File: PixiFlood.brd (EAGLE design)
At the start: 47 x 47 mm, 31 parts, among them IC1 78L05Z, IC2 WS2811-SOP8, IC3 TC7W04FTC7W04F, U1 PT4115PT4115B89E, U2 PT4115PT4115B89E, U3 PT4115PT4115B89E, X1 22-23-2031, X2 LED-PAD, X3 LED-PAD, X4 22-23-2031, X5 LED-PAD, X6 LED-PAD, X7 LED-PAD, X8 LED-PAD

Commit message: Reworked and retitled to PixiFlood
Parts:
- D1, D2, D3: value (none) -> 1N5819
- IC2: value WS2811-SOP8 -> WS2811SOP8; device MyLibrary:SO08-SKINNYPADS -> drivers:SOP08-P-1.27
- IC3: value TC7W04FTC7W04F -> TC7W04F; device MyLibrary:SO08 -> logic:SOP08-P-1.27
- L1, L2, L3: value SLF7045 -> 82114R; device inductors:SLF7045 -> inductors:82114R
- R1, R6: device resistor:R1206 -> resistor:0204/5
- R2, R3, R4: device rcl:M0805 -> rcl:0204/5
- R5: device resistor:M1206 -> resistor:0204/5
- U1, U2, U3: value PT4115PT4115B89E -> PT4115B89E; device IC:SOT89-5 -> drivers:SOT89-5
- moved C1 24.6 mm to (43.7, 35.9), turned to 180 degrees
- moved L3 3.05 mm to (35.6, 7.49), turned to 90 degrees
- moved L1 2.84 mm to (35.3, 23.1), turned to 90 degrees
- moved L2 2.81 mm to (35.4, 15.4), turned to 90 degrees
- moved IC1 2.22 mm to (43.8, 39.9), turned to 270 degrees
- moved R6 2.18 mm to (19.2, 7.95)
- moved R5 1.82 mm to (19.3, 15.8)
- moved C2 1.73 mm to (38.5, 40.8)
- moved R3 1.48 mm to (34.0, 37.5)
- moved X1 1.27 mm to (24.1, 42.5)
- moved X4 1.02 mm to (32.0, 42.5)
- moved R1 0.76 mm to (21.1, 25.5)
- moved R2 0.65 mm to (27.1, 38.1)
- moved IC2 0.51 mm to (34.3, 33.8)
- moved R4 0.51 mm to (34.3, 30.0)
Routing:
- net +12V: track 87.5 -> 93.9 mm
- net RED: track 19.2 -> 23.6 mm, vias 2 -> 0
- net N$19: track 31.8 -> 27.6 mm
- net BLUE: track 23.7 -> 20.0 mm
- net N$10: track 42.6 -> 38.9 mm
- net N$9: track 57.4 -> 54.0 mm
- net GREEN: track 21.3 -> 18.0 mm
- net ROUT: track 45.2 -> 48.1 mm
- net N$1: track 8.89 -> 6.73 mm
- net N$7: track 3.88 -> 1.93 mm
- net N$2: track 8.80 -> 6.94 mm
- net +5V: track 51.7 -> 53.6 mm
- net N$5: track 8.67 -> 6.84 mm
- net N$3: track 63.9 -> 62.1 mm
- net GOUT: track 49.0 -> 50.2 mm
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
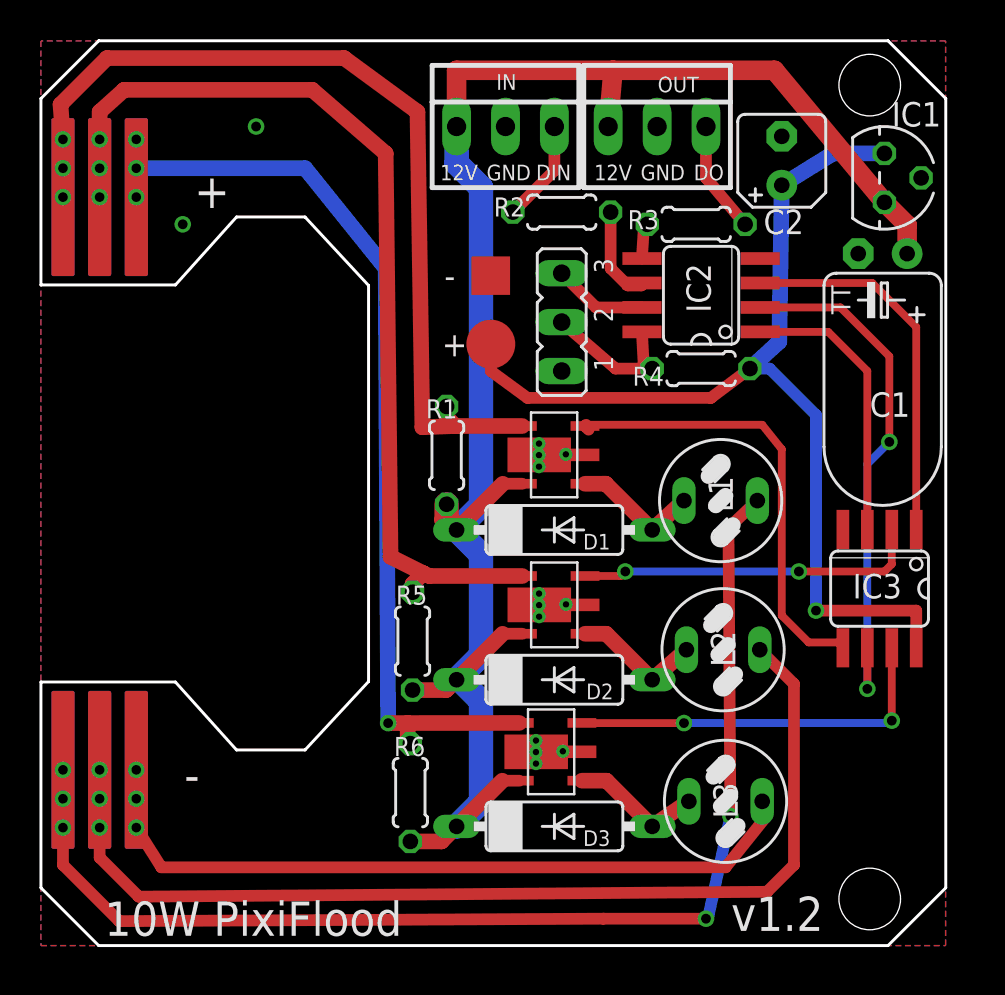
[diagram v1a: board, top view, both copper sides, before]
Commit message: Reworked and retitled to PixiFlood SMD
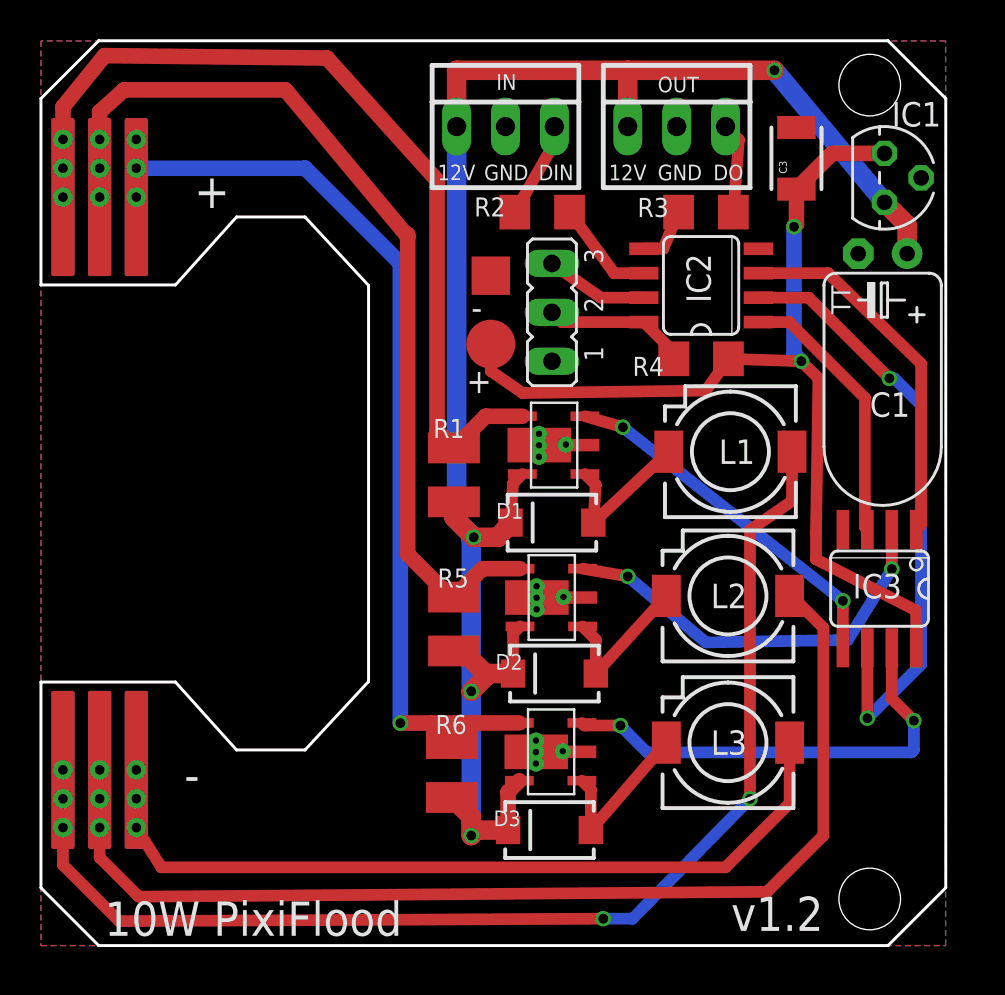
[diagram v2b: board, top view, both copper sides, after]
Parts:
- removed C2: .1uF, resistor:B45181A
- added C3: .1uF, SparkFun-Capacitors:1210
- D1, D2, D3: value 1N5819 -> B340A; device diode:DO07 -> SparkFun-DiscreteSemi:SMA-DIODE
- IC1: value 78L05Z -> AS78L05ZTR-E1
- IC2: value WS2811SOP8 -> WS2811-SOP8; device drivers:SOP08-P-1.27 -> MyLibrary:SO08-SKINNYPADS
- IC3: value TC7W04F -> TC7W04FTC7W04F; device logic:SOP08-P-1.27 -> MyLibrary:SO08
- L1, L2, L3: value 82114R -> SLF7045T-101MR60-H; device inductors:82114R -> inductors:SLF7045
- R1, R6: value .3ohm .25w -> .3ohm .5w; device resistor:0204/5 -> resistor:R1210
- R2, R3, R4: device rcl:0204/5 -> rcl:R1206
- R5: value .3hm .25w -> .3hm .5w; device resistor:0204/5 -> resistor:R1210
- U1, U2, U3: value PT4115B89E -> PT4115PT4115B89E; device drivers:SOT89-5 -> IC:SOT89-5
- moved L3 3.05 mm to (35.7, 10.5), turned to 0 degrees
- moved L2 2.81 mm to (35.7, 18.2), turned to 0 degrees
- moved L1 2.59 mm to (35.8, 25.7), turned to 0 degrees
- moved R6 2.44 mm to (21.3, 9.09)
- moved R5 2.33 mm to (21.5, 16.7)
- moved R1 1.09 mm to (21.5, 24.4)
- moved X4 1.02 mm to (33.0, 42.5)
- moved R2 1.02 mm to (26.0, 38.1)
- moved R3 0.81 mm to (34.5, 38.1)
- moved JP1 0.72 mm to (26.5, 32.9)
- moved IC2 0.51 mm to (34.3, 34.3)
- moved R4 0.51 mm to (34.3, 30.5)
- moved U1 0.51 mm to (26.7, 26.1)
- moved D1 0.40 mm to (26.5, 22.0), turned to 180 degrees
- moved U2 0.40 mm to (26.5, 18.2)
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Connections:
- net +5V: now also C3.1; no longer C2.+
- net GND: now also C3.2; no longer C2.-
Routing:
- net RED: track 23.6 -> 19.0 mm, vias 0 -> 2
- net N$19: track 27.6 -> 31.8 mm
- net BLUE: track 20.0 -> 23.7 mm
- net N$10: track 38.9 -> 42.6 mm
- net N$9: track 54.0 -> 57.4 mm
- net GREEN: track 18.0 -> 21.5 mm
- net +5V: track 53.6 -> 51.7 mm, vias 1 -> 2
- net N$2: track 6.94 -> 8.76 mm
- net GOUT: track 50.2 -> 48.4 mm
- net N$3: track 62.1 -> 63.6 mm
- net N$1: track 6.73 -> 8.14 mm
- net N$5: track 6.84 -> 8.18 mm
- net ROUT: track 48.1 -> 46.7 mm
- net N$7: track 1.93 -> 3.07 mm
- net N$4: track 5.82 -> 4.74 mm
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
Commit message: Reworked layout
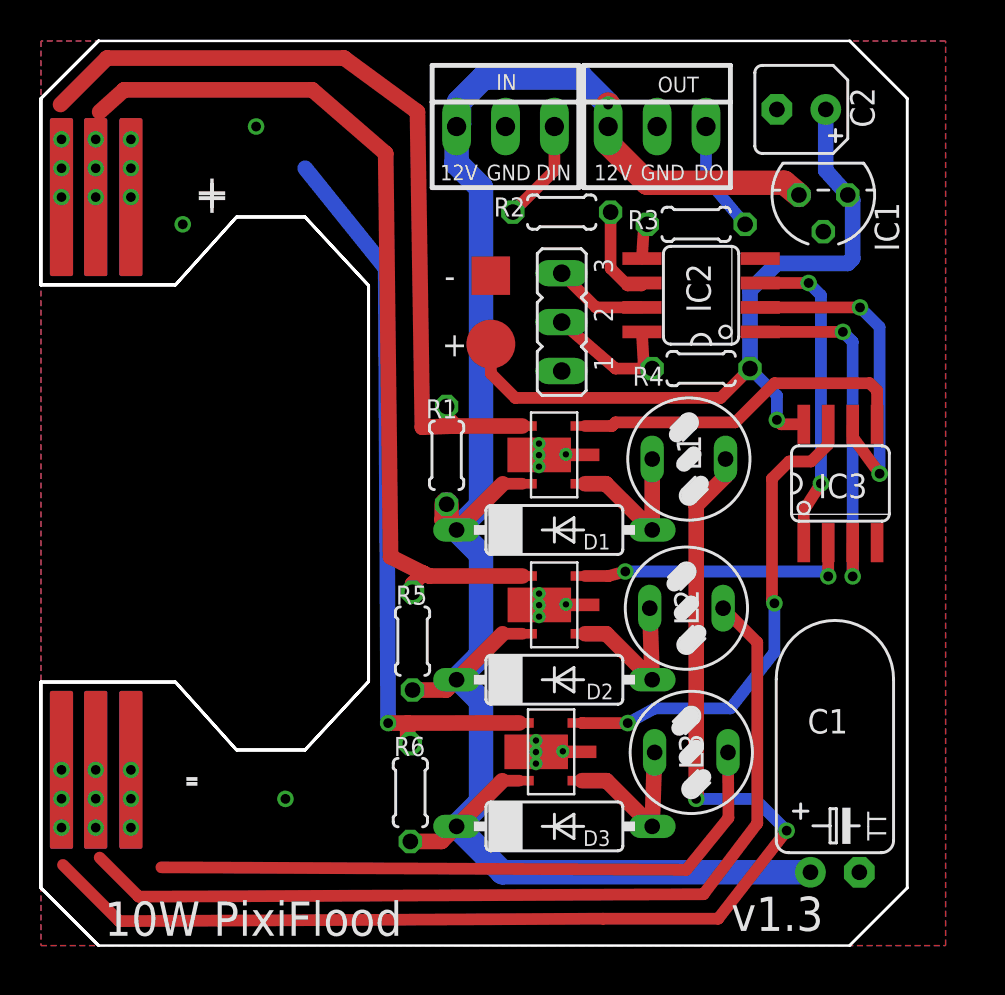
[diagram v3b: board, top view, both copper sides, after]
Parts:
- removed C3: .1uF, SparkFun-Capacitors:1210
- removed X2, X3, X5, X6, X7, X8: LED-PAD, MyLibrary:LED-PAD
- added B1: LED-BOARDV2, special:LED-BOARD_V2
- added C2: .1uF, resistor:B45181A
- D1, D2, D3: value B340A -> 1N5819; device SparkFun-DiscreteSemi:SMA-DIODE -> diode:DO07
- IC1: value AS78L05ZTR-E1 -> 78L05Z
- IC2: value WS2811-SOP8 -> WS2811SOP8; device MyLibrary:SO08-SKINNYPADS -> drivers:SOP08-P-1.27
- IC3: value TC7W04FTC7W04F -> TC7W04F; device MyLibrary:SO08 -> logic:SOP08-P-1.27
- L1, L2, L3: value SLF7045T-101MR60-H -> 82114R; device inductors:SLF7045 -> inductors:82114R
- R1, R6: value .3ohm .5w -> .3ohm .25w; device resistor:R1210 -> resistor:0204/5
- R2, R3, R4: device rcl:R1206 -> rcl:0204/5
- R5: value .3hm .5w -> .3hm .25w; device resistor:R1210 -> resistor:0204/5
- U1, U2, U3: value PT4115PT4115B89E -> PT4115B89E; device IC:SOT89-5 -> drivers:SOT89-5
- moved C1 32.2 mm to (41.2, 3.81), turned to 0 degrees
- moved IC3 5.83 mm to (41.5, 24.0), turned to 0 degrees
- moved IC1 3.30 mm to (40.6, 39.0), turned to 180 degrees
- moved R6 2.44 mm to (19.2, 7.95)
- moved R5 2.33 mm to (19.3, 15.8)
- moved L2 2.25 mm to (33.5, 17.5), turned to 90 degrees
- moved L1 2.19 mm to (33.7, 25.3), turned to 90 degrees
- moved L3 1.97 mm to (33.8, 10.0), turned to 90 degrees
- moved R1 1.09 mm to (21.1, 25.5)
- moved X4 1.02 mm to (32.0, 42.5)
- moved R2 1.02 mm to (27.1, 38.1)
- moved R3 0.81 mm to (34.0, 37.5)
- moved JP1 0.72 mm to (27.1, 32.4)
- moved IC2 0.51 mm to (34.3, 33.8)
- moved R4 0.51 mm to (34.3, 30.0)
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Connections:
- net +5V: now also C2.+; no longer C3.1
- net BOUT: now also B1.P$5@1, B1.P$5@2, B1.P$5@3; no longer X7.P$1@1, X7.P$1@2, X7.P$1@3
- net GND: now also C2.-; no longer C3.2
- net GOUT: now also B1.P$3@1, B1.P$3@2, B1.P$3@3; no longer X5.P$1@1, X5.P$1@2, X5.P$1@3
- net N$10: now also B1.P$6@1, B1.P$6@2, B1.P$6@3; no longer X8.P$1@1, X8.P$1@2, X8.P$1@3
- net N$3: now also B1.P$2@1, B1.P$2@2, B1.P$2@3; no longer X3.P$1@1, X3.P$1@2, X3.P$1@3
- net N$9: now also B1.P$4@1, B1.P$4@2, B1.P$4@3; no longer X6.P$1@1, X6.P$1@2, X6.P$1@3
- net ROUT: now also B1.P$1@1, B1.P$1@2, B1.P$1@3; no longer X2.P$1@1, X2.P$1@2, X2.P$1@3
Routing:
- net N$19: track 31.8 -> 17.3 mm
- net +5V: track 51.7 -> 39.3 mm, vias 2 -> 1
- net BOUT: track 50.1 -> 38.2 mm
- net N$9: track 57.4 -> 48.7 mm
- net N$10: track 42.6 -> 34.1 mm
- net +12V: track 93.6 -> 102.0 mm, vias 4 -> 1
- net GREEN: track 21.5 -> 14.5 mm
- net N$15: track 14.1 -> 19.0 mm, vias 0 -> 2
- net ROUT: track 46.7 -> 43.2 mm
- net GOUT: track 48.4 -> 45.8 mm
- net N$16: track 19.1 -> 16.5 mm, vias 0 -> 2
- net BLUE: track 23.7 -> 25.4 mm
- net N$7: track 3.07 -> 1.93 mm
- net N$4: track 4.74 -> 5.82 mm
- net N$3: track 63.6 -> 64.7 mm
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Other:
- board size 47 x 47 mm -> 45 x 47 mm
- board text added: "v1.3"
- board text removed: "v1.2"

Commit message: Reworked layout
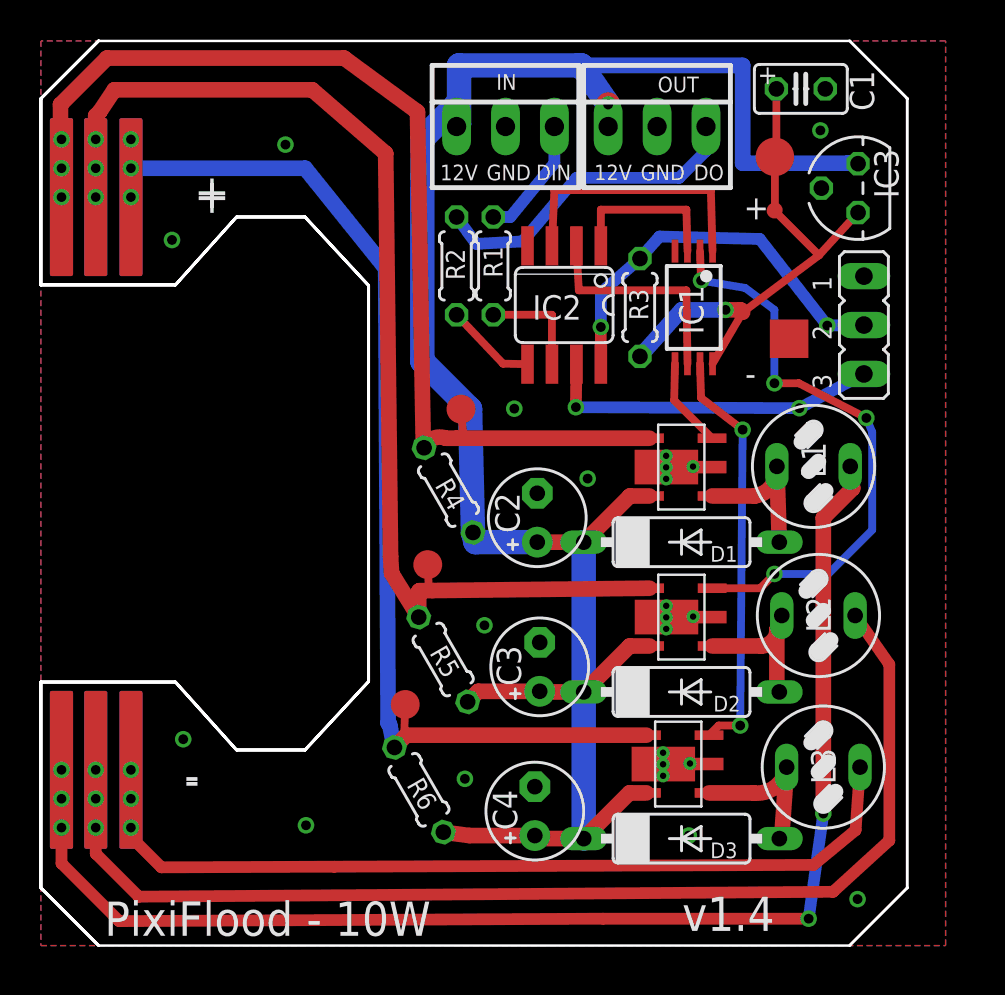
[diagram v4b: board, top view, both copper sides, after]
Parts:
- added C3, C4: 10uF, adafruit:E2,5-5
- added TP3, TP5, TP7: TPSQTP15R, testpad:TP15R
- C1: value EL 100uF -> .1uF; device rcl:TT2D6L -> capacitors:C025X050P
- C2: value .1uF -> 10uF; device resistor:B45181A -> adafruit:E2,5-5
- IC1: value 78L05Z -> TC7W04FP-0.65; device linear:TO92 -> logic:TSSOP8
- IC3: value TC7W04F -> 78L05Z; device logic:SOP08-P-1.27 -> linear:TO92
- R1: value .3ohm .25w -> 33R; device resistor:0204/5 -> rcl:0204/5
- R3: value 33R -> 100ohm
- R4: value 100ohm -> .3ohm .25w; device rcl:0204/5 -> resistor:0204/5
- TP1: value TPB2,54 -> TPSQTP20R; device testpad:B2,54 -> testpad:TP20R
- TP2: value PTR1TP20SQ -> TPSQTP20SQ
- moved C1 40.7 mm to (39.5, 44.5)
- moved C2 25.3 mm to (25.8, 22.2), turned to 90 degrees
- moved TP1 17.7 mm to (38.1, 41.0)
- moved TP2 15.8 mm to (38.9, 31.5)
- moved JP1 15.7 mm to (42.7, 32.2), turned to 270 degrees
- moved IC3 15.4 mm to (42.4, 39.3), turned to 90 degrees
- moved R4 14.6 mm to (21.2, 23.7), turned to 300 degrees
- moved R1 10.1 mm to (23.5, 35.3)
- moved IC1 8.91 mm to (33.9, 33.1), turned to 270 degrees
- moved IC2 7.13 mm to (27.2, 33.3), turned to 180 degrees
- moved L3 6.90 mm to (40.6, 9.27)
- moved L2 6.87 mm to (40.4, 17.1)
- moved D1 6.63 mm to (33.3, 21.0)
- moved D2 6.63 mm to (33.3, 13.2)
- moved D3 6.63 mm to (33.3, 5.56)
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- renumbered X4 to X2
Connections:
- net +12V: now also C2.+, C3.+, C4.+, IC3.3, R4.2; no longer C1.+, IC1.3, R1.2
- net +5V: now also C1.1, IC1.8, IC3.1, R3.1; no longer C2.+, IC1.1, IC3.8, R4.1
- net BLUE: now also IC1.7; no longer IC3.7
- net BOUT: now also TP7.TP
- net GND: now also C1.2, C3.-, C4.-, IC1.4, IC3.2; no longer C1.-, IC1.2, IC3.4
- net GOUT: now also TP5.TP
- net GREEN: now also IC1.2; no longer IC3.2
- net N$14: now also R3.2; no longer R4.2
- net N$15: now also IC1.3; no longer IC3.3
- net N$16: now also IC1.1; no longer IC3.1
- net N$19: now also IC1.6; no longer IC3.6
- net N$4: now also R2.1; no longer R3.1
- net N$6: now also R1.1; no longer R2.1
- net N$7: now also R2.2; no longer R3.2
- net N$8: now also R1.2; no longer R2.2
- net RED: now also IC1.5; no longer IC3.5
- net ROUT: now also R4.1, TP3.TP; no longer R1.1
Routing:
- net BOUT: track 38.2 -> 58.7 mm, vias 1 -> 0
- net GREEN: track 14.5 -> 30.2 mm, vias 2 -> 4
- net GOUT: track 45.8 -> 60.5 mm
- net RED: track 18.0 -> 4.68 mm
- net ROUT: track 43.2 -> 56.2 mm
- net N$14: track 7.89 -> 20.8 mm, vias 0 -> 2
- net N$18: track 4.90 -> 17.6 mm, vias 0 -> 2
- net +5V: track 39.3 -> 27.2 mm
- net N$10: track 34.1 -> 45.7 mm
- net N$4: track 5.82 -> 17.0 mm
- net N$9: track 48.7 -> 59.8 mm
- net N$15: track 19.0 -> 8.48 mm, vias 2 -> 0
- net N$19: track 17.3 -> 11.7 mm, vias 2 -> 0
- net N$3: track 64.7 -> 69.1 mm
- net BLUE: track 25.4 -> 21.7 mm
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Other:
- board text added: "PixiFlood - 10W"
- board text added: "v1.4"
- board text removed: "10W PixiFlood"
- board text removed: "v1.3"

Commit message: Reworked layout
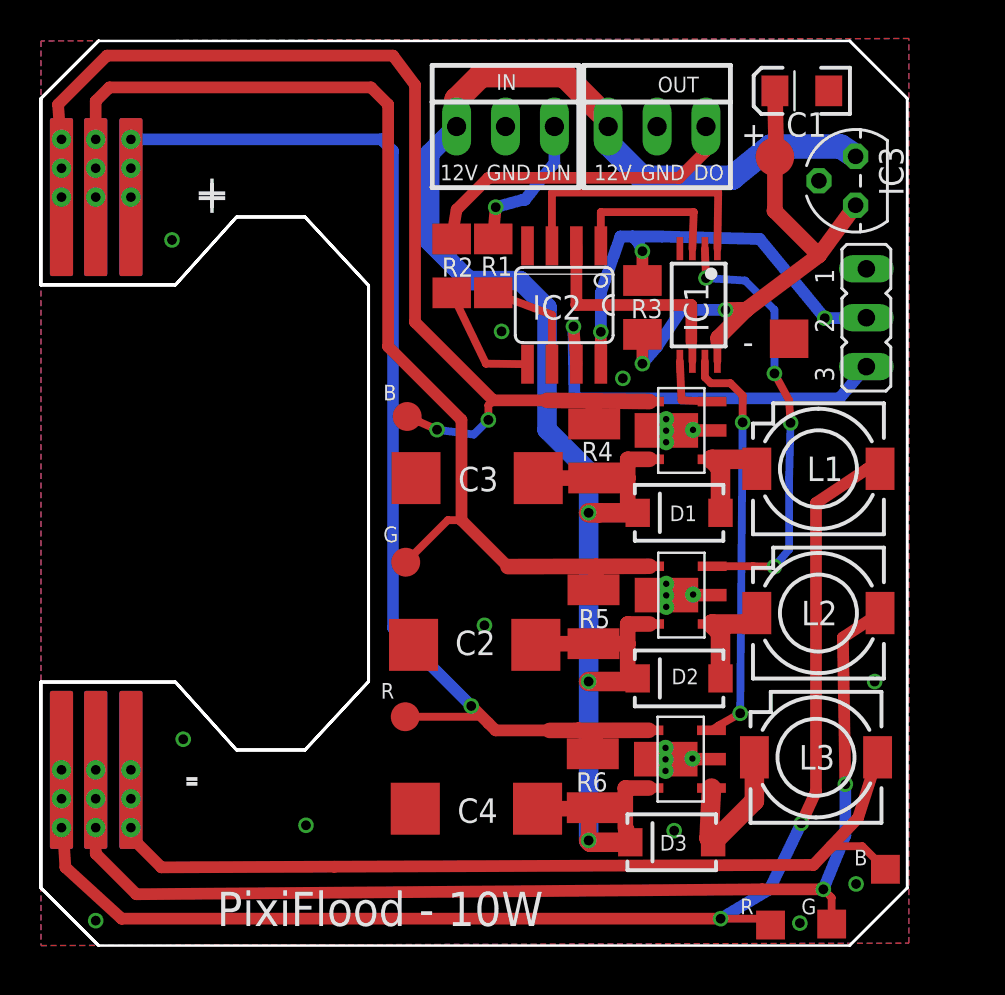
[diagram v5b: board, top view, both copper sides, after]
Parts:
- added TP6, TP8, TP9: TPSQTP15SQ, testpad:TP15SQ
- C1: device capacitors:C025X050P -> capacitors:EIA3216
- C2, C3, C4: device adafruit:E2,5-5 -> capacitors:D/7343-31R
- D1, D2, D3: value 1N5819 -> MBRA140; device diode:DO07 -> SparkFun-DiscreteSemi:SMA-DIODE
- L1, L2, L3: value 82114R -> SLF7045T-101MR60-H; device inductors:82114R -> inductors:SLF7045
- R1, R2, R3: device rcl:0204/5 -> rcl:M1206
- R4, R5, R6: device resistor:0204/5 -> resistor:R1210
- moved C3 10.3 mm to (22.7, 24.3), turned to 0 degrees
- moved R6 9.05 mm to (28.7, 8.56), turned to 270 degrees
- moved R5 8.12 mm to (28.7, 17.1), turned to 270 degrees
- moved R4 7.83 mm to (28.7, 25.7), turned to 270 degrees
- moved C2 7.36 mm to (22.5, 15.6), turned to 0 degrees
- moved C4 3.04 mm to (22.6, 7.11), turned to 0 degrees
- moved TP3 2.82 mm to (19.0, 27.5)
- moved U1 1.91 mm to (33.3, 26.8)
- moved D1 1.53 mm to (33.1, 22.5), turned to 180 degrees
- moved TP5 1.15 mm to (18.9, 19.9)
- moved U2 1.14 mm to (33.3, 18.3)
- moved D2 0.71 mm to (33.1, 13.9), turned to 180 degrees
- moved TP7 0.63 mm to (18.9, 11.9)
- moved L3 0.63 mm to (40.3, 9.78), turned to 0 degrees
- moved D3 0.54 mm to (32.8, 5.37), turned to 180 degrees
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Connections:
- net +5V: now also C1.A; no longer C1.1
- net GND: now also C1.C; no longer C1.2
- net N$10: now also TP6.TP
- net N$3: now also TP9.TP
- net N$9: now also TP8.TP
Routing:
- net GREEN: track 30.2 -> 22.8 mm
- net BOUT: track 58.7 -> 63.6 mm, vias 0 -> 1
- net N$18: track 17.6 -> 21.6 mm, vias 2 -> 1
- net N$10: track 45.7 -> 49.6 mm
- net N$14: track 20.8 -> 24.0 mm, vias 2 -> 3
- net N$1: track 8.07 -> 5.49 mm
- net N$5: track 7.77 -> 5.56 mm
- net ROUT: track 56.2 -> 58.4 mm, vias 0 -> 2
- net +5V: track 27.2 -> 29.2 mm, vias 1 -> 2
- net +12V: track 105.4 -> 103.6 mm, vias 1 -> 3
- net N$7: track 4.77 -> 6.25 mm
- net N$3: track 69.1 -> 70.3 mm
- net N$6: track 6.40 -> 7.57 mm, vias 0 -> 1
- net RED: track 4.68 -> 3.62 mm
- net N$9: track 59.8 -> 60.6 mm, vias 0 -> 2
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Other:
- board text added: "B"
- board text added: "G"
- board text added: "R"
- board text added: "V1.4"
- board text removed: "v1.4"
